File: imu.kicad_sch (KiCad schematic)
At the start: 6 parts, among them U6 LSM9DS1

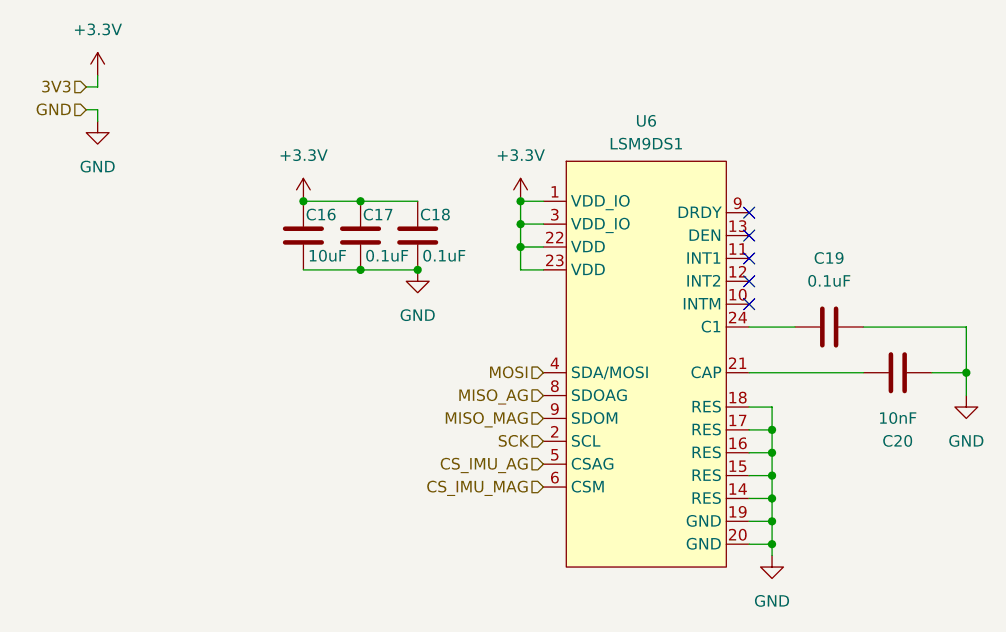
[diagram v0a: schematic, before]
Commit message: Added IMU schematic
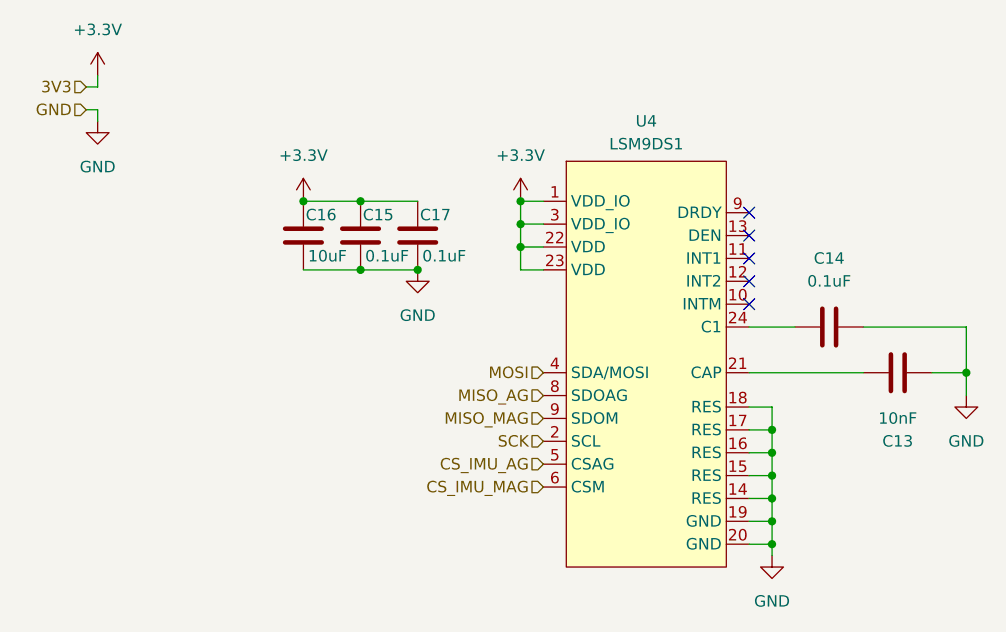
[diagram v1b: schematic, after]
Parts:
- renumbered C20 to C13, C19 to C14, C17 to C15, C18 to C17, U6 to U4
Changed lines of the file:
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@@
 		(dnp no)
 		(fields_autoplaced yes)
-		(property "Reference" "U6"
+		(property "Reference" "U4"
 			(at 114.3 39.37 0)
 			(effects
@@
 			(project ""
 				(path "/2c2eadf0-5503-4531-8753-1a232087fe8c/b9b0c40a-7771-4bc1-adbf-abe0201c34d0/6214bd7c-f0f2-4cad-9d95-7bb7bb29e083"
-					(reference "U6")
+					(reference "U4")
 					(unit 1)
 				)
@@
 		(dnp no)
 		(fields_autoplaced yes)
-		(property "Reference" "#PWR071"
+		(property "Reference" "#PWR059"
 			(at 76.2 52.07 0)
 			(effects
@@
 			(project ""
 				(path "/2c2eadf0-5503-4531-8753-1a232087fe8c/b9b0c40a-7771-4bc1-adbf-abe0201c34d0/6214bd7c-f0f2-4cad-9d95-7bb7bb29e083"
-					(reference "#PWR071")
+					(reference "#PWR059")
 					(unit 1)
 				)
@@
 		(dnp no)
 		(fields_autoplaced yes)
-		(property "Reference" "#PWR072"
+		(property "Reference" "#PWR056"
 			(at 100.33 52.07 0)
 			(effects
@@
 			(project ""
 				(path "/2c2eadf0-5503-4531-8753-1a232087fe8c/b9b0c40a-7771-4bc1-adbf-abe0201c34d0/6214bd7c-f0f2-4cad-9d95-7bb7bb29e083"
-					(reference "#PWR072")
+					(reference "#PWR056")
 					(unit 1)
 				)
@@
 		(dnp no)
 		(fields_autoplaced yes)
-		(property "Reference" "#PWR070"
+		(property "Reference" "#PWR053"
 			(at 53.34 45.72 0)
 			(effects
@@
 			(project ""
 				(path "/2c2eadf0-5503-4531-8753-1a232087fe8c/b9b0c40a-7771-4bc1-adbf-abe0201c34d0/6214bd7c-f0f2-4cad-9d95-7bb7bb29e083"
-					(reference "#PWR070")
+					(reference "#PWR053")
 					(unit 1)
 				)
@@
 		(dnp no)
 		(fields_autoplaced yes)
-		(property "Reference" "#PWR075"
+		(property "Reference" "#PWR055"
 			(at 128.27 93.98 0)
 			(effects
@@
 			(project ""
 				(path "/2c2eadf0-5503-4531-8753-1a232087fe8c/b9b0c40a-7771-4bc1-adbf-abe0201c34d0/6214bd7c-f0f2-4cad-9d95-7bb7bb29e083"
-					(reference "#PWR075")
+					(reference "#PWR055")
 					(unit 1)
 				)
@@
 		(dnp no)
 		(fields_autoplaced yes)
-		(property "Reference" "#PWR074"
+		(property "Reference" "#PWR057"
 			(at 149.86 76.2 0)
 			(effects
@@
 			(project ""
 				(path "/2c2eadf0-5503-4531-8753-1a232087fe8c/b9b0c40a-7771-4bc1-adbf-abe0201c34d0/6214bd7c-f0f2-4cad-9d95-7bb7bb29e083"
-					(reference "#PWR074")
+					(reference "#PWR057")
 					(unit 1)
 				)
@@
 		(on_board yes)
 		(dnp no)
-		(property "Reference" "C18"
+		(property "Reference" "C17"
 			(at 89.154 49.784 0)
 			(effects
@@
 			(project ""
 				(path "/2c2eadf0-5503-4531-8753-1a232087fe8c/b9b0c40a-7771-4bc1-adbf-abe0201c34d0/6214bd7c-f0f2-4cad-9d95-7bb7bb29e083"
-					(reference "C18")
+					(reference "C17")
 					(unit 1)
 				)
@@
 		(on_board yes)
 		(dnp no)
-		(property "Reference" "C17"
+		(property "Reference" "C15"
 			(at 82.804 49.784 0)
 			(effects
@@
 			(project ""
 				(path "/2c2eadf0-5503-4531-8753-1a232087fe8c/b9b0c40a-7771-4bc1-adbf-abe0201c34d0/6214bd7c-f0f2-4cad-9d95-7bb7bb29e083"
-					(reference "C17")
+					(reference "C15")
 					(unit 1)
 				)
@@
 		(dnp no)
 		(fields_autoplaced yes)
-		(property "Reference" "C19"
+		(property "Reference" "C14"
 			(at 134.62 54.61 90)
 			(effects
@@
 			(project ""
 				(path "/2c2eadf0-5503-4531-8753-1a232087fe8c/b9b0c40a-7771-4bc1-adbf-abe0201c34d0/6214bd7c-f0f2-4cad-9d95-7bb7bb29e083"
-					(reference "C19")
+					(reference "C14")
 					(unit 1)
 				)
@@
 		(on_board yes)
 		(dnp no)
-		(property "Reference" "C20"
+		(property "Reference" "C13"
 			(at 142.24 74.93 90)
 			(effects
@@
 			(project ""
 				(path "/2c2eadf0-5503-4531-8753-1a232087fe8c/b9b0c40a-7771-4bc1-adbf-abe0201c34d0/6214bd7c-f0f2-4cad-9d95-7bb7bb29e083"
-					(reference "C20")
+					(reference "C13")
 					(unit 1)
 				)
@@
 		(dnp no)
 		(fields_autoplaced yes)
-		(property "Reference" "#PWR073"
+		(property "Reference" "#PWR060"
 			(at 88.9 62.23 0)
 			(effects
@@
 			(project ""
 				(path "/2c2eadf0-5503-4531-8753-1a232087fe8c/b9b0c40a-7771-4bc1-adbf-abe0201c34d0/6214bd7c-f0f2-4cad-9d95-7bb7bb29e083"
-					(reference "#PWR073")
+					(reference "#PWR060")
 					(unit 1)
 				)
@@
 		(dnp no)
 		(fields_autoplaced yes)
-		(property "Reference" "#PWR069"
+		(property "Reference" "#PWR054"
 			(at 53.34 38.1 0)
 			(effects
@@
 			(project ""
 				(path "/2c2eadf0-5503-4531-8753-1a232087fe8c/b9b0c40a-7771-4bc1-adbf-abe0201c34d0/6214bd7c-f0f2-4cad-9d95-7bb7bb29e083"
-					(reference "#PWR069")
-					(unit 1)
-				)
+					(reference "#PWR054")
+					(unit 1)
+				)

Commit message: Reannotated
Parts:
- renumbered C15 to C17, C17 to C18, C14 to C19, C13 to C20, U4 to U6
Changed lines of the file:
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@@
 		(dnp no)
 		(fields_autoplaced yes)
-		(property "Reference" "U4"
+		(property "Reference" "U6"
 			(at 114.3 39.37 0)
 			(effects
@@
 			(project ""
 				(path "/2c2eadf0-5503-4531-8753-1a232087fe8c/b9b0c40a-7771-4bc1-adbf-abe0201c34d0/6214bd7c-f0f2-4cad-9d95-7bb7bb29e083"
-					(reference "U4")
+					(reference "U6")
 					(unit 1)
 				)
@@
 		(dnp no)
 		(fields_autoplaced yes)
-		(property "Reference" "#PWR059"
+		(property "Reference" "#PWR071"
 			(at 76.2 52.07 0)
 			(effects
@@
 			(project ""
 				(path "/2c2eadf0-5503-4531-8753-1a232087fe8c/b9b0c40a-7771-4bc1-adbf-abe0201c34d0/6214bd7c-f0f2-4cad-9d95-7bb7bb29e083"
-					(reference "#PWR059")
+					(reference "#PWR071")
 					(unit 1)
 				)
@@
 		(dnp no)
 		(fields_autoplaced yes)
-		(property "Reference" "#PWR056"
+		(property "Reference" "#PWR072"
 			(at 100.33 52.07 0)
 			(effects
@@
 			(project ""
 				(path "/2c2eadf0-5503-4531-8753-1a232087fe8c/b9b0c40a-7771-4bc1-adbf-abe0201c34d0/6214bd7c-f0f2-4cad-9d95-7bb7bb29e083"
-					(reference "#PWR056")
+					(reference "#PWR072")
 					(unit 1)
 				)
@@
 		(dnp no)
 		(fields_autoplaced yes)
-		(property "Reference" "#PWR053"
+		(property "Reference" "#PWR070"
 			(at 53.34 45.72 0)
 			(effects
@@
 			(project ""
 				(path "/2c2eadf0-5503-4531-8753-1a232087fe8c/b9b0c40a-7771-4bc1-adbf-abe0201c34d0/6214bd7c-f0f2-4cad-9d95-7bb7bb29e083"
-					(reference "#PWR053")
+					(reference "#PWR070")
 					(unit 1)
 				)
@@
 		(dnp no)
 		(fields_autoplaced yes)
-		(property "Reference" "#PWR055"
+		(property "Reference" "#PWR075"
 			(at 128.27 93.98 0)
 			(effects
@@
 			(project ""
 				(path "/2c2eadf0-5503-4531-8753-1a232087fe8c/b9b0c40a-7771-4bc1-adbf-abe0201c34d0/6214bd7c-f0f2-4cad-9d95-7bb7bb29e083"
-					(reference "#PWR055")
+					(reference "#PWR075")
 					(unit 1)
 				)
@@
 		(dnp no)
 		(fields_autoplaced yes)
-		(property "Reference" "#PWR057"
+		(property "Reference" "#PWR074"
 			(at 149.86 76.2 0)
 			(effects
@@
 			(project ""
 				(path "/2c2eadf0-5503-4531-8753-1a232087fe8c/b9b0c40a-7771-4bc1-adbf-abe0201c34d0/6214bd7c-f0f2-4cad-9d95-7bb7bb29e083"
-					(reference "#PWR057")
+					(reference "#PWR074")
 					(unit 1)
 				)
@@
 		(on_board yes)
 		(dnp no)
-		(property "Reference" "C17"
+		(property "Reference" "C18"
 			(at 89.154 49.784 0)
 			(effects
@@
 			(project ""
 				(path "/2c2eadf0-5503-4531-8753-1a232087fe8c/b9b0c40a-7771-4bc1-adbf-abe0201c34d0/6214bd7c-f0f2-4cad-9d95-7bb7bb29e083"
-					(reference "C17")
+					(reference "C18")
 					(unit 1)
 				)
@@
 		(on_board yes)
 		(dnp no)
-		(property "Reference" "C15"
+		(property "Reference" "C17"
 			(at 82.804 49.784 0)
 			(effects
@@
 			(project ""
 				(path "/2c2eadf0-5503-4531-8753-1a232087fe8c/b9b0c40a-7771-4bc1-adbf-abe0201c34d0/6214bd7c-f0f2-4cad-9d95-7bb7bb29e083"
-					(reference "C15")
+					(reference "C17")
 					(unit 1)
 				)
@@
 		(dnp no)
 		(fields_autoplaced yes)
-		(property "Reference" "C14"
+		(property "Reference" "C19"
 			(at 134.62 54.61 90)
 			(effects
@@
 			(project ""
 				(path "/2c2eadf0-5503-4531-8753-1a232087fe8c/b9b0c40a-7771-4bc1-adbf-abe0201c34d0/6214bd7c-f0f2-4cad-9d95-7bb7bb29e083"
-					(reference "C14")
+					(reference "C19")
 					(unit 1)
 				)
@@
 		(on_board yes)
 		(dnp no)
-		(property "Reference" "C13"
+		(property "Reference" "C20"
 			(at 142.24 74.93 90)
 			(effects
@@
 			(project ""
 				(path "/2c2eadf0-5503-4531-8753-1a232087fe8c/b9b0c40a-7771-4bc1-adbf-abe0201c34d0/6214bd7c-f0f2-4cad-9d95-7bb7bb29e083"
-					(reference "C13")
+					(reference "C20")
 					(unit 1)
 				)
@@
 		(dnp no)
 		(fields_autoplaced yes)
-		(property "Reference" "#PWR060"
+		(property "Reference" "#PWR073"
 			(at 88.9 62.23 0)
 			(effects
@@
 			(project ""
 				(path "/2c2eadf0-5503-4531-8753-1a232087fe8c/b9b0c40a-7771-4bc1-adbf-abe0201c34d0/6214bd7c-f0f2-4cad-9d95-7bb7bb29e083"
-					(reference "#PWR060")
+					(reference "#PWR073")
 					(unit 1)
 				)
@@
 		(dnp no)
 		(fields_autoplaced yes)
-		(property "Reference" "#PWR054"
+		(property "Reference" "#PWR069"
 			(at 53.34 38.1 0)
 			(effects
@@
 			(project ""
 				(path "/2c2eadf0-5503-4531-8753-1a232087fe8c/b9b0c40a-7771-4bc1-adbf-abe0201c34d0/6214bd7c-f0f2-4cad-9d95-7bb7bb29e083"
-					(reference "#PWR054")
-					(unit 1)
-				)
+					(reference "#PWR069")
+					(unit 1)
+				)

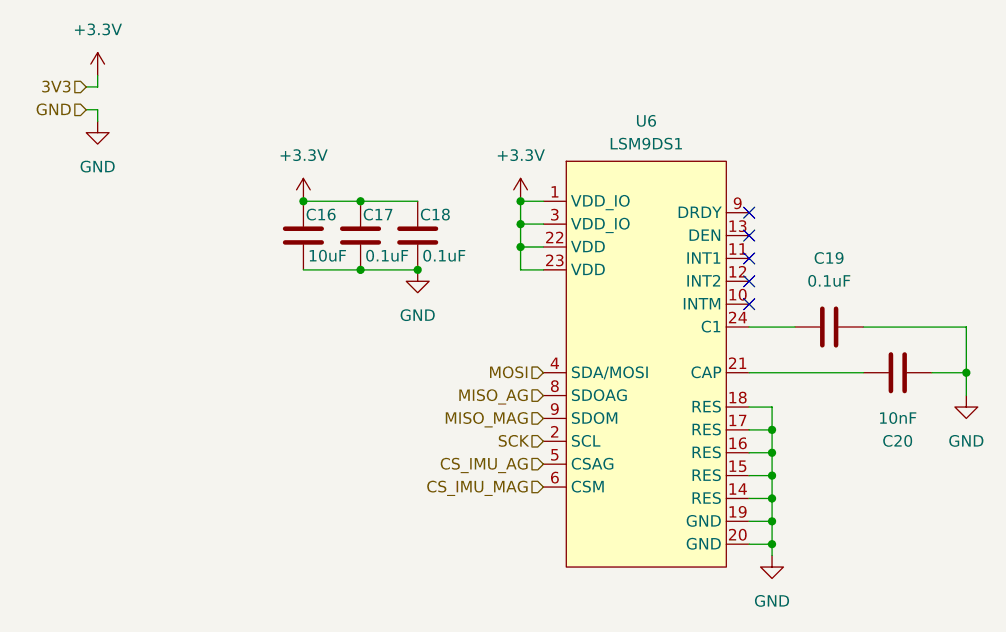
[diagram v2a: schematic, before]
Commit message: Connected topsheet
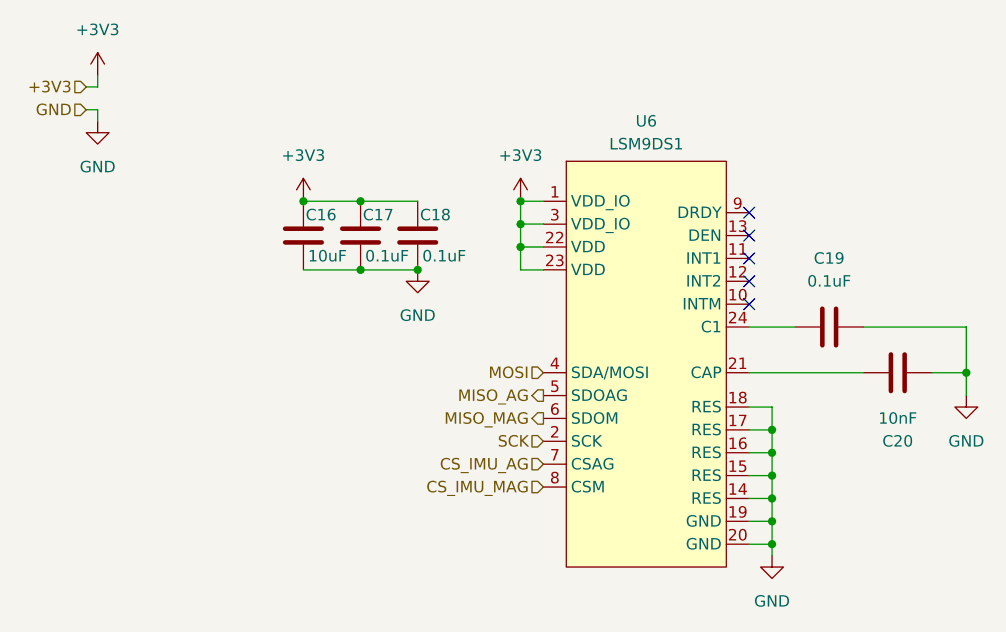
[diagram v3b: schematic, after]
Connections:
- net CS_IMU_AG: now also U6.7 (CSAG); no longer U6.5 (CSAG)
- net CS_IMU_MAG: now also U6.8 (CSM); no longer U6.6 (CSM)
- net MISO_AG: now also U6.5 (SDOAG); no longer U6.8 (SDOAG)
- net MISO_MAG: now also U6.6 (SDOM); no longer U6.9 (DRDY)
- net +3.3V renamed +3V3
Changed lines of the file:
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@@
 	)
 	(hierarchical_label "MISO_MAG"
-		(shape input)
+		(shape output)
 		(at 102.87 72.39 180)
 		(effects
@@
 		)
 	)
-	(hierarchical_label "3V3"
+	(hierarchical_label "+3V3"
 		(shape input)
 		(at 52.07 35.56 180)
@@
 	)
 	(hierarchical_label "MISO_AG"
-		(shape input)
+		(shape output)
 		(at 102.87 69.85 180)
 		(effects
@@
 		(pin "6"
 		)
-		(pin "9"
+		(pin "7"
 		)
 		(pin "13"
@@
 			)
 		)
-		(property "Value" "+3.3V"
+		(property "Value" "+3V3"
 			(at 76.2 43.18 0)
 			(effects
@@
 			)
 		)
-		(property "Value" "+3.3V"
+		(property "Value" "+3V3"
 			(at 100.33 43.18 0)
 			(effects
@@
 			)
 		)
-		(property "Value" "+3.3V"
+		(property "Value" "+3V3"
 			(at 53.34 29.21 0)
 			(effects

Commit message: Footprint selection
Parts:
- C16, C17, C18, C19, C20: footprint (none) -> Capacitor_SMD:C_0603_1608Metric
- U6: footprint (none) -> Avionics_Feet:PQFN24P43_350X300X102L35X23N
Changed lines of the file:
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@@
 			)
 		)
-		(property "Footprint" ""
+		(property "Footprint" "Capacitor_SMD:C_0603_1608Metric"
 			(at 77.1652 55.88 0)
 			(effects
@@
 			)
 		)
-		(property "Footprint" ""
+		(property "Footprint" "Avionics_Feet:PQFN24P43_350X300X102L35X23N"
 			(at 101.6 40.64 0)
 			(effects
@@
 			)
 		)
-		(property "Footprint" ""
+		(property "Footprint" "Capacitor_SMD:C_0603_1608Metric"
 			(at 89.8652 55.88 0)
 			(effects
@@
 			)
 		)
-		(property "Footprint" ""
+		(property "Footprint" "Capacitor_SMD:C_0603_1608Metric"
 			(at 83.5152 55.88 0)
 			(effects
@@
 			)
 		)
-		(property "Footprint" ""
+		(property "Footprint" "Capacitor_SMD:C_0603_1608Metric"
 			(at 130.81 63.1952 0)
 			(effects
@@
 			)
 		)
-		(property "Footprint" ""
+		(property "Footprint" "Capacitor_SMD:C_0603_1608Metric"
 			(at 146.05 68.2752 0)
 			(effects
